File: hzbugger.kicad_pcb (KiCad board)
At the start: 2 copper layers, 53.5 x 26.7 mm, 56 parts, among them J2 IDC, J4 SWD, J6 GPIO, SW1 RESET_SW, SW2 BOOT0_SW, U1 STM32F103C8T6, U2 SRV05-4, U3 AMS1117-3.3, U4 HX AM 90D, Y1 8M

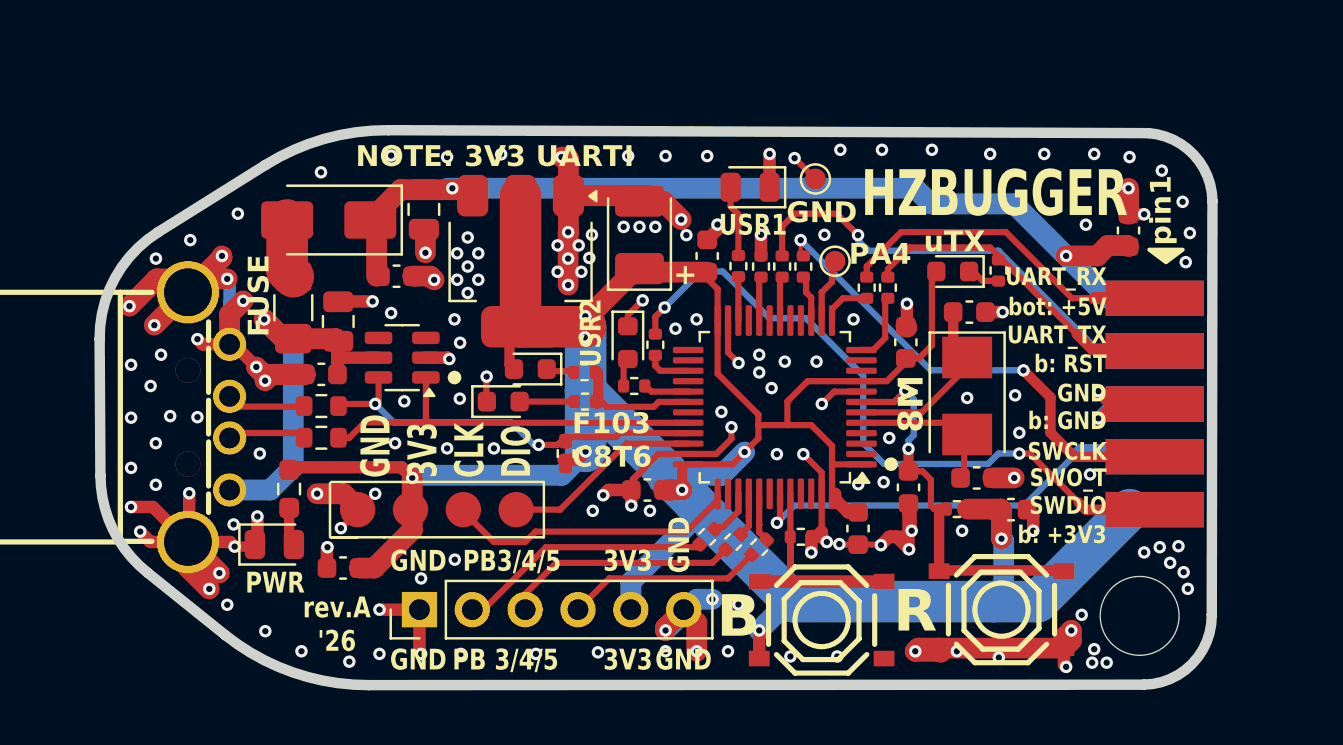
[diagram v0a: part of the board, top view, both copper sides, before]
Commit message: pinout enhancements, layout, physical outline + gitignore updateg
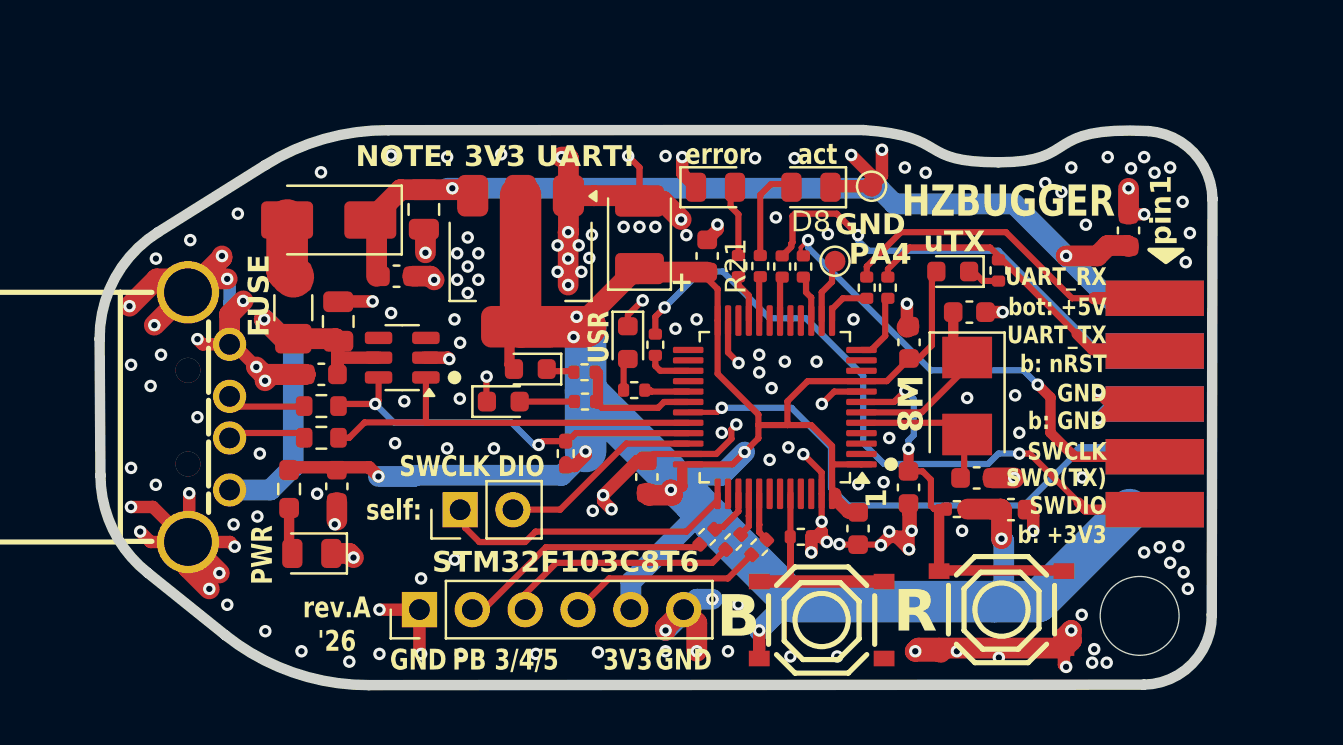
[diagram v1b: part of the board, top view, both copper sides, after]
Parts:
- removed J4: SWD, hzbugger:SMD-PinHeader_1x04_P2.54mm_Vertical
- removed R12: 10k, Resistor_SMD:R_0402_1005Metric
- added D8: ACT_LED, LED_SMD:LED_0805_2012Metric, F.Cu at (135.0, 76.2)
- added J1: SELF_SWD, Connector_PinHeader_2.54mm:PinHeader_1x02_P2.54mm_Vertical, F.Cu at (118.1, 91.7)
- added R21: 1k5, Resistor_SMD:R_0402_1005Metric, F.Cu at (132.6, 80.0)
- D6: value LED1 -> ERR_LED
- moved C2 3.94 mm to (112.2, 90.6), turned to -90 degrees
- moved TP2 2.72 mm to (137.9, 76.2)
- moved D1 1.85 mm to (111.0, 93.8), turned to 180 degrees
- moved D6 1.66 mm to (130.4, 76.2), turned to 0 degrees
- moved C10 0.63 mm to (127.1, 90.1), turned to 90 degrees
- moved R18 0.20 mm to (126.5, 86.0)
- moved C9 0.15 mm to (139.7, 83.7)
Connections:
- R19 pad 1: Net-(U1-PB11) -> Net-(U1-PB10)
- U1 pad 21: unconnected-(U1-PB10-Pad21) -> Net-(U1-PB10)
- U1 pad 22: Net-(U1-PB11) -> unconnected-(U1-PB11-Pad22)
- U1 pad 31: unconnected-(U1-PA10-Pad31) -> SWO_TRACE
- U1 pad 43: SWO_TRACE -> unconnected-(U1-PB7-Pad43)
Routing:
- net SWO_TRACE: track 21.9 -> 27.5 mm
- net Net-(D8-A): track 0.00 -> 4.68 mm
- net +3V3: track 148.0 -> 143.3 mm
- net Net-(U1-PB10): track 0.00 -> 2.31 mm
- net Net-(U1-PB11): track 2.11 -> 0.00 mm
- net GND: track 145.3 -> 144.6 mm, vias 168 -> 170
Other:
- outline, holes or cut-outs redrawn
- board text added: "1"
- board text added: "STM32F103C8T6"
- board text added: "SWCLK DIO"
- board text added: "USR"
- board text added: "act"
- board text added: "bot: +5V b: nRST b: GND SWO(TX) b: +3V3"
- board text added: "error"
- board text added: "self:"
- board text removed: "F103 C8T6"
- board text removed: "GND 3V3 CLK DIO"
- board text removed: "PB3/4/5"
- board text removed: "USR1"
- board text removed: "USR2"
- board text removed: "bot: +5V b: RST b: GND SWO_T b: +3V3"

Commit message: form factor, mounting holes
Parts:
- added H1: MountingHole, MountingHole:MountingHole_2.1mm, F.Cu at (103.6, 76.5)
- added H2: MountingHole_Pad, MountingHole:MountingHole_2.1mm, F.Cu at (103.7, 97.1)
- moved C14 9.96 mm to (140.5, 76.2)
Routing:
- net GND: track 144.6 -> 141.6 mm, vias 170 -> 173
- net +5V: track 48.5 -> 46.6 mm
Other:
- board size 53.5 x 26.7 mm -> 53.7 x 28.4 mm
- board text added: "NOTE: 3V3 UART"
- board text added: "PB3/4/5"
- board text added: "hzb"
- board text added: "p1"
- board text removed: "NOTE: 3V3 UART!"
- board text removed: "PB 3/4/5"
- board text removed: "pin1"

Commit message: some fine-tuning
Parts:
- moved R13 1.33 mm to (122.8, 86.5)
- moved R3 0.31 mm to (124.1, 85.4)
- moved R18 0.18 mm to (126.6, 85.8)
- moved C9 0.10 mm to (139.6, 83.7)
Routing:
- net LED_LINK: track 6.23 -> 8.30 mm
- net Net-(D3-A): track 2.63 -> 1.30 mm
- net GND: track 141.6 -> 142.3 mm, vias 173 -> 181
- net Net-(SW1-A): track 19.1 -> 18.5 mm
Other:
- board text added: "aux"
- board text removed: "USR"

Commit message: some finalisation, schema style etc
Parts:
- added H3: MountingHole_Pad, MountingHole:MountingHole_2.1mm, F.Cu at (150.6, 96.4)
- added R12: 10k, Resistor_SMD:R_0402_1005Metric, F.Cu at (139.2, 80.8)
- D2: value SS34 -> SS14
- D6, D8: footprint LED_SMD:LED_0805_2012Metric -> LED_SMD:LED_0603_1608Metric
- moved R10 4.15 mm to (140.8, 78.2), turned to 0 degrees
- moved R9 1.40 mm to (138.0, 82.2)
- moved R20 0.20 mm to (144.0, 80.0)
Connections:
- U1 pad 11: unconnected-(U1-PA1-Pad11) -> Net-(U1-PA1)
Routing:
- net Net-(U1-PA1): track 0.00 -> 4.79 mm
- net UART_RX: track 16.3 -> 11.6 mm
- net Net-(U1-PA3): track 2.43 -> 6.98 mm
- net UART_TX: track 13.3 -> 15.2 mm
- net Net-(U1-PA2): track 3.28 -> 1.78 mm
- net GND: track 142.3 -> 143.4 mm, vias 181 -> 179
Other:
- board text added: "PLEASE NOTE: 3V3 UART!"
- board text added: "act."
- board text removed: "NOTE: 3V3 UART"
- board text removed: "act"
